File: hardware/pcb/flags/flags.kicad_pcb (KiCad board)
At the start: 2 copper layers, 62.2 x 21.6 mm, 42 parts, among them J1 Bus, J2 Control, J3 Sync, J4 Power, J5 Flags_Bus, J6 Ctrl_Out, U1 74HC02, U2 74HC08, U3 74HC157, U4 74HC173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

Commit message: Corrected footprints for Flags, needs re-routing
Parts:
- U3, U4, U5: footprint Package_SO:SOIC-16W_5.3x10.2mm_P1.27mm -> Package_SO:SOIC-16_3.9x9.9mm_P1.27mm

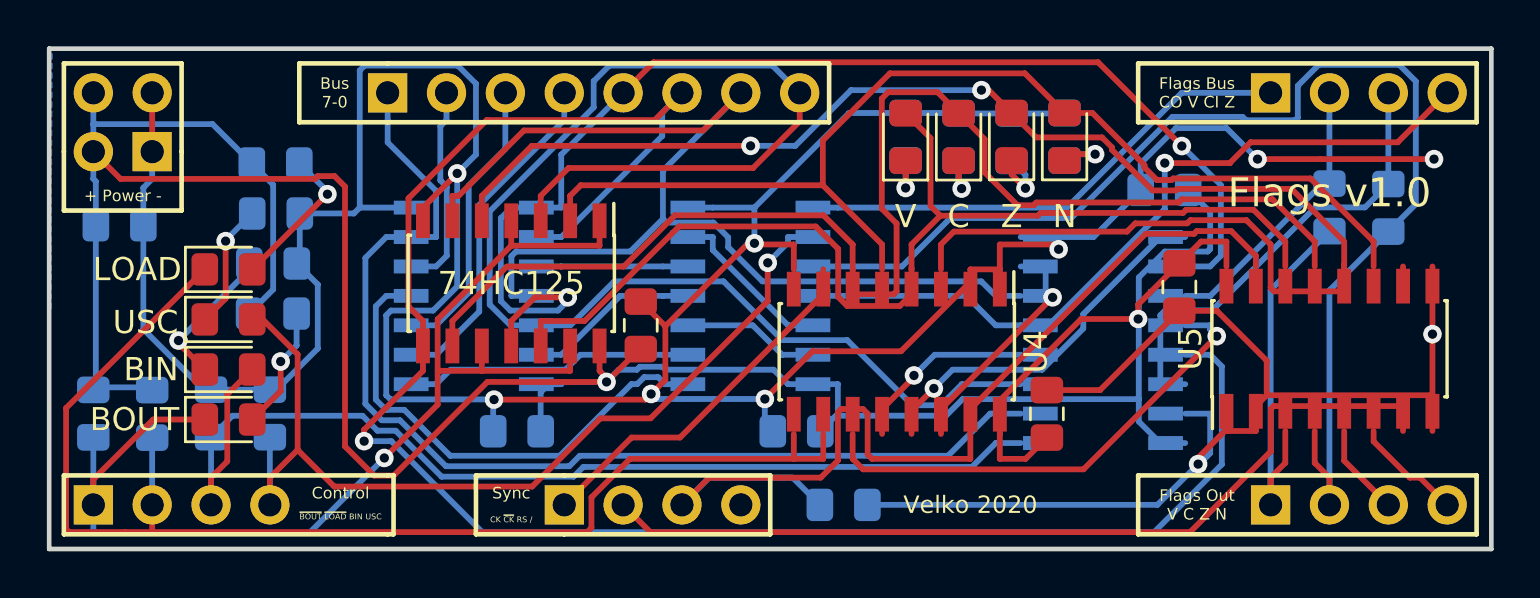
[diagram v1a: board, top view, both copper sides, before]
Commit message: Quick and ugly reroute (checkpoint)
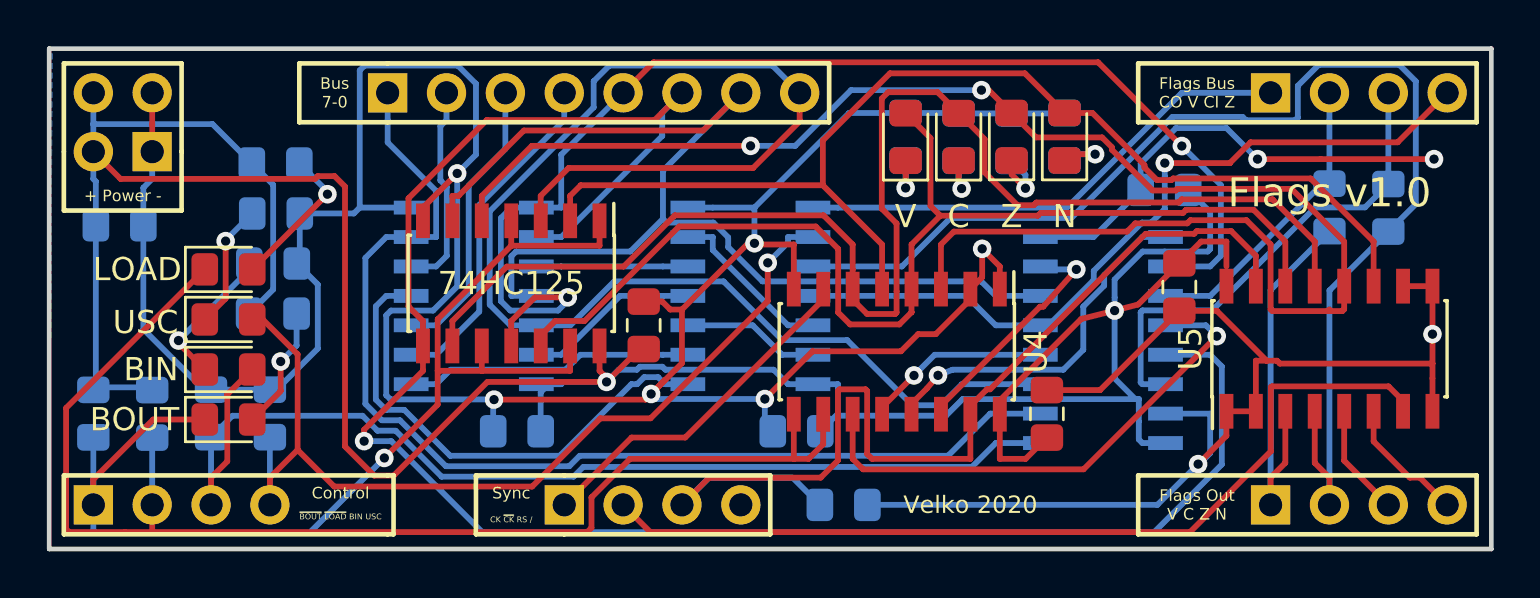
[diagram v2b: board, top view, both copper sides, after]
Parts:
- moved C4 0.13 mm to (60.6, 48.1)
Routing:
- net Z_D: track 66.4 -> 69.3 mm
- net RST: track 42.8 -> 45.5 mm
- net C_D: track 57.0 -> 59.5 mm
- net V_D: track 47.2 -> 49.2 mm
- net C_I: track 21.0 -> 22.6 mm
- net N_D: track 48.0 -> 49.4 mm
- net ~LOAD~: track 54.7 -> 56.0 mm
- net CARRY_IN: track 20.2 -> 21.2 mm
- net SEL: track 46.5 -> 47.4 mm
- net OV_IN: track 12.1 -> 13.0 mm
- net BUS3: track 53.1 -> 53.9 mm
- net BUS2: track 80.8 -> 81.6 mm
- net BUS0: track 62.6 -> 63.5 mm
- net BUS7: track 47.1 -> 48.0 mm
- net Z_CTRL: track 3.98 -> 4.83 mm
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
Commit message: Removed all tracks
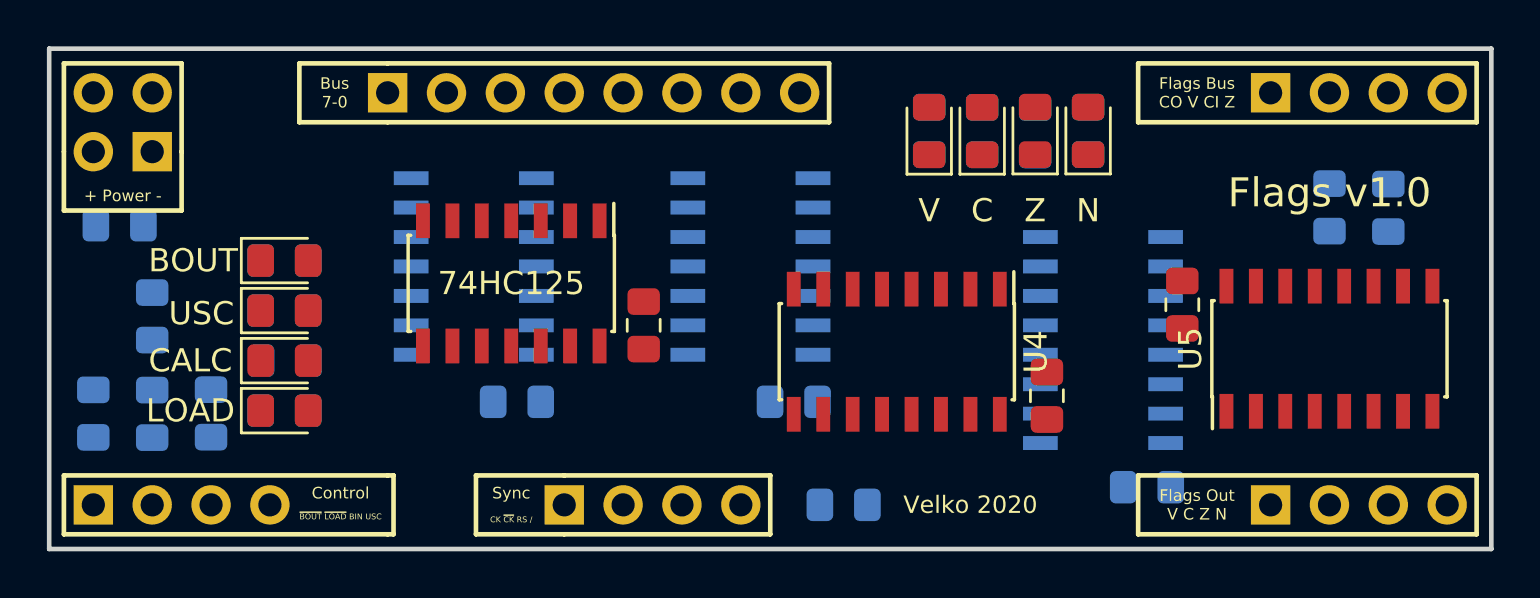
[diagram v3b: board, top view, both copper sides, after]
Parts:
- C7: value 10μF -> 10uF
- D5: value BOUT -> LOAD
- D6: value LOAD -> BOUT
- D7: value BIN -> CALC
- moved C3 12.8 mm to (82.3, 55.1)
- moved R8 10.7 mm to (45.1, 51.8)
- moved R13 4.90 mm to (39.4, 47.7), turned to 90 degrees
- moved R9 4.22 mm to (45.1, 49.7), turned to 0 degrees
- moved R10 4.21 mm to (45.1, 47.5)
- moved R14 2.54 mm to (41.9, 51.9)
- moved D5 2.44 mm to (45.1, 51.8)
- moved D6 2.44 mm to (45.1, 45.3)
- moved D7 2.44 mm to (45.1, 49.7)
- moved D8 2.44 mm to (45.1, 47.5)
- moved R7 2.34 mm to (45.1, 45.3)
- moved C1 1.28 mm to (67.1, 51.4)
- moved C2 1.27 mm to (55.1, 51.4)
- moved U1 1.27 mm to (53.2, 45.6)
- moved U2 1.27 mm to (65.2, 45.6)
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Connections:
- D5 pad 1: ~OUT~ -> ~B_LOAD~
- D6 pad 1: ~LOAD~ -> ~OUT~
- D7 pad 1: Net-(D7-Pad1) -> ~B_CALC~
- D7 pad 2: SEL -> Net-(D7-Pad2)
- D8 pad 2: USE_CARRY -> CARRY_OUT
- J2 pad 2: ~LOAD~ -> ~B_LOAD~
- J2 pad 3: SEL -> ~B_CALC~
- J2 pad 4: USE_CARRY -> CARRY_OUT
- R12 pad 2: ~LOAD~ -> ~B_LOAD~
- R13 pad 1: GND -> VCC
- R13 pad 2: SEL -> ~B_CALC~
- R14 pad 2: USE_CARRY -> CARRY_OUT
- R7 pad 2: Net-(D5-Pad2) -> Net-(D6-Pad2)
- R8 pad 2: Net-(D6-Pad2) -> Net-(D5-Pad2)
- R9 pad 1: GND -> VCC
- R9 pad 2: Net-(D7-Pad1) -> Net-(D7-Pad2)
- U2 pad 10: C_CTRL -> ~B_CALC~
- U2 pad 8: CARRY_OUT -> ~LATCH~
- U2 pad 9: USE_CARRY -> ~B_LOAD~
- U3 pad 1: SEL -> ~B_LOAD~
- U3 pad 10: BUS3 -> BUS7
- U3 pad 11: OV_IN -> BUS0
- U3 pad 12: C_I -> Z_I
- U3 pad 13: BUS2 -> Z_OUT
- U3 pad 14: CARRY_IN -> BUS1
- U3 pad 2: BUS7 -> BUS3
- U3 pad 3: BUS0 -> OV_IN
- U3 pad 4: N_I -> V_I
- U3 pad 5: Z_OUT -> BUS2
- U3 pad 6: BUS1 -> CARRY_IN
- U3 pad 7: Z_I -> C_I
- U3 pad 9: V_I -> N_I
- U4 pad 10: ~LOAD~ -> ~LATCH~
- U4 pad 11: C_I -> N_I
- U4 pad 12: N_I -> Z_I
- U4 pad 13: V_I -> C_I
- U4 pad 14: Z_I -> V_I
- U4 pad 3: Z_D -> V_D
- U4 pad 4: V_D -> C_D
- U4 pad 5: N_D -> Z_D
- U4 pad 6: C_D -> N_D
- U4 pad 9: ~LOAD~ -> ~LATCH~
- U6 pad 11: BUS3 -> BUS1
- U6 pad 12: V_D -> Z_D
- U6 pad 5: Z_D -> V_D
- U6 pad 6: BUS1 -> BUS3
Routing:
- net GND: track 202.9 -> 0.00 mm, vias 10 -> 0
- net VCC: track 136.4 -> 0.00 mm, vias 2 -> 0
- net BUS2: track 81.6 -> 0.00 mm, vias 1 -> 0
- net Z_D: track 69.3 -> 0.00 mm, vias 2 -> 0
- net BUS0: track 63.5 -> 0.00 mm
- net C_D: track 59.5 -> 0.00 mm
- net ~LOAD~: track 56.0 -> 0.00 mm
- net C_CTRL: track 55.0 -> 0.00 mm
- net BUS3: track 53.9 -> 0.00 mm, vias 2 -> 0
- net ~OUT~: track 50.5 -> 0.00 mm, vias 1 -> 0
- net BUS1: track 49.9 -> 0.00 mm
- net N_D: track 49.4 -> 0.00 mm
- net V_D: track 49.2 -> 0.00 mm
- net BUS7: track 48.0 -> 0.00 mm
- net SEL: track 47.4 -> 0.00 mm
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- removed copper zone on B.Cu, net GND
- removed copper zone on F.Cu, net VCC

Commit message: Moved around for easier routing
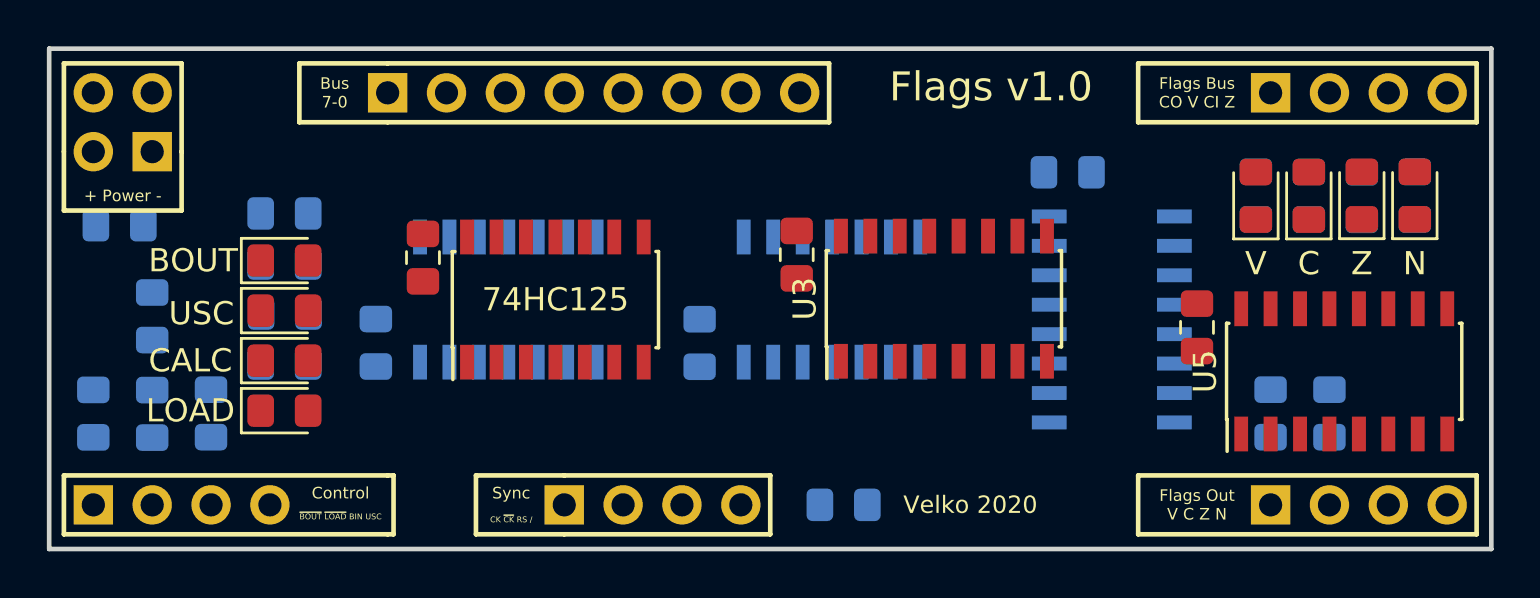
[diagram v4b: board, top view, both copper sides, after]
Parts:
- C3, U3: moved to F.Cu
- C5, U4: moved to B.Cu
- moved C3 18.1 mm to (67.2, 45.1), turned to 270 degrees
- moved D2 14.4 mm to (87.0, 42.5)
- moved D4 14.4 mm to (89.3, 42.5)
- moved R4 14.4 mm to (87.0, 42.5)
- moved R6 14.4 mm to (89.3, 42.5)
- moved D1 14.4 mm to (91.6, 42.5)
- moved D3 14.4 mm to (93.9, 42.5)
- moved R3 14.4 mm to (91.6, 42.6)
- moved R5 14.4 mm to (93.9, 42.5)
- moved C4 9.96 mm to (51.1, 45.2), turned to 270 degrees
- moved C5 9.68 mm to (78.9, 41.5), turned to 0 degrees
- moved U4 9.38 mm to (80.8, 47.9), turned to 180 degrees
- moved R2 9.25 mm to (87.6, 51.9)
- moved R1 9.23 mm to (90.2, 51.9)
- moved U3 7.09 mm to (73.5, 47.0), turned to 90 degrees
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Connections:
- U1 pad 11: BUS1 -> BUS4
- U1 pad 12: BUS0 -> BUS6
- U1 pad 2: BUS4 -> BUS7
- U1 pad 5: BUS6 -> BUS3
- U1 pad 6: BUS7 -> BUS2
- U1 pad 8: BUS3 -> BUS0
- U1 pad 9: BUS2 -> BUS1
- U2 pad 10: ~B_CALC~ -> ~B_LOAD~
- U2 pad 11: Z_OUT -> Net-(U2-Pad11)
- U2 pad 12: Net-(U2-Pad12) -> Net-(U1-Pad13)
- U2 pad 13: Net-(U2-Pad13) -> Net-(U1-Pad10)
- U2 pad 3: Net-(U2-Pad13) -> Net-(U2-Pad3)
- U2 pad 4: Net-(U1-Pad13) -> Net-(U2-Pad11)
- U2 pad 5: Net-(U1-Pad10) -> Net-(U2-Pad3)
- U2 pad 6: Net-(U2-Pad12) -> Z_OUT
- U2 pad 9: ~B_LOAD~ -> ~B_CALC~
- U6 pad 2: N_D -> C_D
- U6 pad 3: BUS0 -> BUS2
- U6 pad 8: BUS2 -> BUS0
- U6 pad 9: C_D -> N_D
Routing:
- added copper zone on B.Cu, net GND
- added copper zone on F.Cu, net VCC

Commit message: Import autorouted
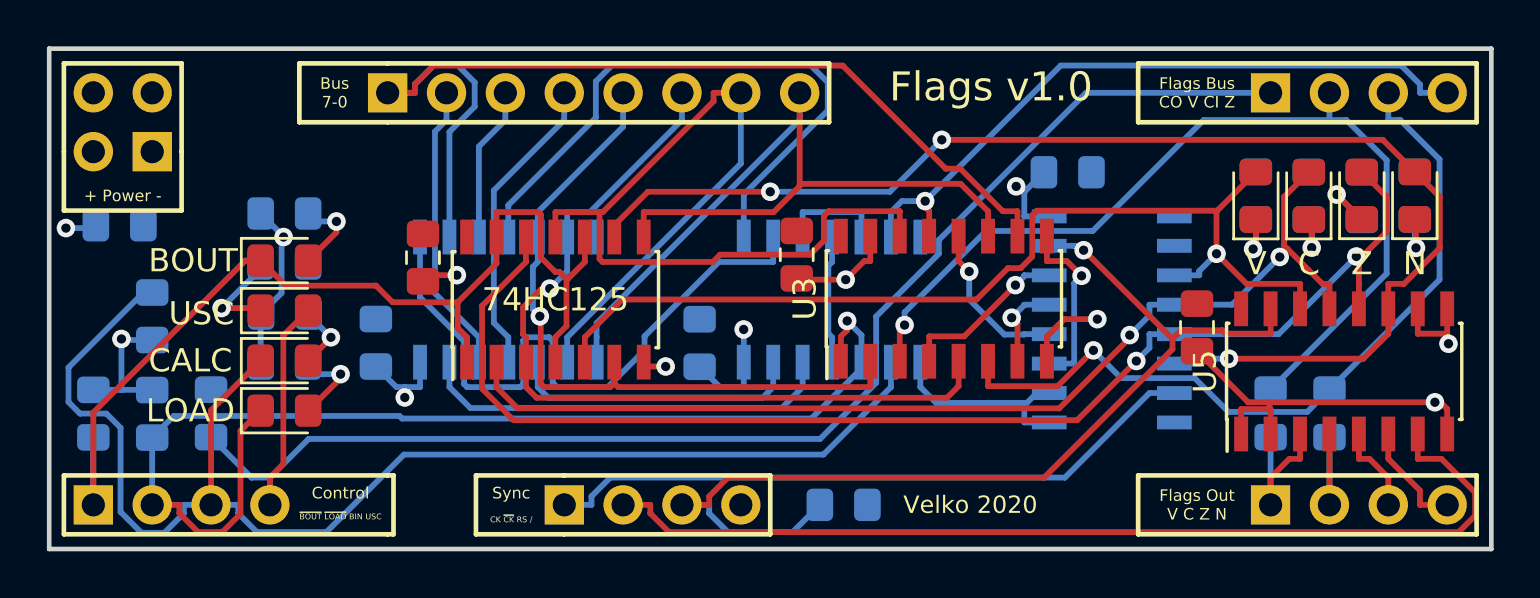
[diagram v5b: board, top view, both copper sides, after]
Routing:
- net CARRY_OUT: track 0.00 -> 65.6 mm
- net ~B_CALC~: track 0.00 -> 58.6 mm
- net Z_D: track 0.00 -> 55.9 mm, vias 0 -> 2
- net N_D: track 0.00 -> 55.7 mm, vias 0 -> 3
- net ~B_LOAD~: track 0.00 -> 48.6 mm, vias 0 -> 1
- net C_D: track 0.00 -> 46.1 mm, vias 0 -> 2
- net ~OUT~: track 0.00 -> 44.7 mm
- net RST: track 0.00 -> 44.3 mm, vias 0 -> 1
- net BUS1: track 0.00 -> 43.8 mm
- net BUS7: track 0.00 -> 43.5 mm
- net V_D: track 0.00 -> 43.4 mm, vias 0 -> 1
- net ~CLK~: track 0.00 -> 42.9 mm
- net OV_IN: track 0.00 -> 40.3 mm, vias 0 -> 1
- net BUS0: track 0.00 -> 37.2 mm
- net BUS2: track 0.00 -> 36.5 mm, vias 0 -> 1
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
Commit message: Connected (checkpoint)
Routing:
- net GND: track 31.3 -> 71.5 mm, vias 6 -> 20
- net VCC: track 27.1 -> 46.2 mm, vias 6 -> 11
- net Net-(U1-Pad4): track 27.1 -> 15.9 mm, vias 0 -> 2
- net BUS1: track 43.8 -> 35.2 mm, vias 0 -> 1
- net BUS0: track 37.2 -> 30.0 mm, vias 0 -> 1
- net ~B_LOAD~: track 48.6 -> 41.6 mm, vias 1 -> 2
- net Net-(U1-Pad1): track 28.1 -> 22.9 mm, vias 0 -> 2
- net ~OUT~: track 44.7 -> 48.4 mm
- net N_D: track 55.7 -> 52.3 mm, vias 3 -> 4
- net CARRY_OUT: track 65.6 -> 68.4 mm
- net OV_IN: track 40.3 -> 42.9 mm
- net V_D: track 43.4 -> 44.7 mm

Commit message: Flags 2.0 finalized
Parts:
- C7: value 10uF -> 10μF
- D8: value USC -> CARRY
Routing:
- net VCC: track 46.2 -> 82.4 mm, vias 11 -> 10
- net GND: track 71.5 -> 94.7 mm, vias 20 -> 22
- net BUS0: track 30.0 -> 28.5 mm
- net Net-(U1-Pad4): track 15.9 -> 14.7 mm
- net N_D: track 52.3 -> 51.3 mm
- net Net-(U1-Pad1): track 22.9 -> 21.9 mm
- net Z_OUT: track 29.8 -> 30.6 mm
- net ~OUT~: track 48.4 -> 47.6 mm
- net Net-(U2-Pad3): track 4.69 -> 3.96 mm
- net N_CTRL: track 4.80 -> 4.11 mm
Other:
- net class Power added: clearance 0.2, trace_width 0.5, via_dia 0.8, via_drill 0.4
- board text added: "CARRY"
- board text added: "CI"
- board text added: "CO"
- board text added: "Flags Bus"
- board text added: "Flags Out"
- board text added: "Flags v2.0"
- board text added: "JLCJLCJLCJLC"
- board text added: "V"
- board text added: "Velko 2021"
- board text added: "Z"
- board text added: "~BOUT~"
- board text added: "~CALC~"
- board text added: "~LOAD~"
- board text removed: "CK ~CK~ RS /"
- board text removed: "Flags Bus CO V CI Z"
- board text removed: "Flags Out V C Z N"
- board text removed: "Flags v1.0"
- board text removed: "Velko 2020"
- board text removed: "~BOUT~ ~LOAD~ BIN USC"

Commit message: Clean tracks again
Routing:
- net GND: track 94.7 -> 0.00 mm, vias 22 -> 0
- net VCC: track 82.4 -> 0.00 mm, vias 10 -> 0
- net CARRY_OUT: track 68.4 -> 0.00 mm
- net ~B_CALC~: track 58.1 -> 0.00 mm
- net Z_D: track 55.6 -> 0.00 mm, vias 2 -> 0
- net N_D: track 51.3 -> 0.00 mm, vias 4 -> 0
- net ~OUT~: track 47.6 -> 0.00 mm
- net C_D: track 45.7 -> 0.00 mm, vias 2 -> 0
- net V_D: track 44.8 -> 0.00 mm, vias 1 -> 0
- net BUS7: track 43.9 -> 0.00 mm
- net RST: track 43.9 -> 0.00 mm, vias 1 -> 0
- net OV_IN: track 42.9 -> 0.00 mm, vias 1 -> 0
- net ~CLK~: track 42.7 -> 0.00 mm
- net ~B_LOAD~: track 41.6 -> 0.00 mm, vias 2 -> 0
- net BUS2: track 36.3 -> 0.00 mm, vias 1 -> 0
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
